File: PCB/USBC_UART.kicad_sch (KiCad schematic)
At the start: 15 parts, among them J1 USB_C_Receptacle_USB2.0_16P, U2 CP2102N-Axx-xQFN20, U3 USBLC6-2SC6

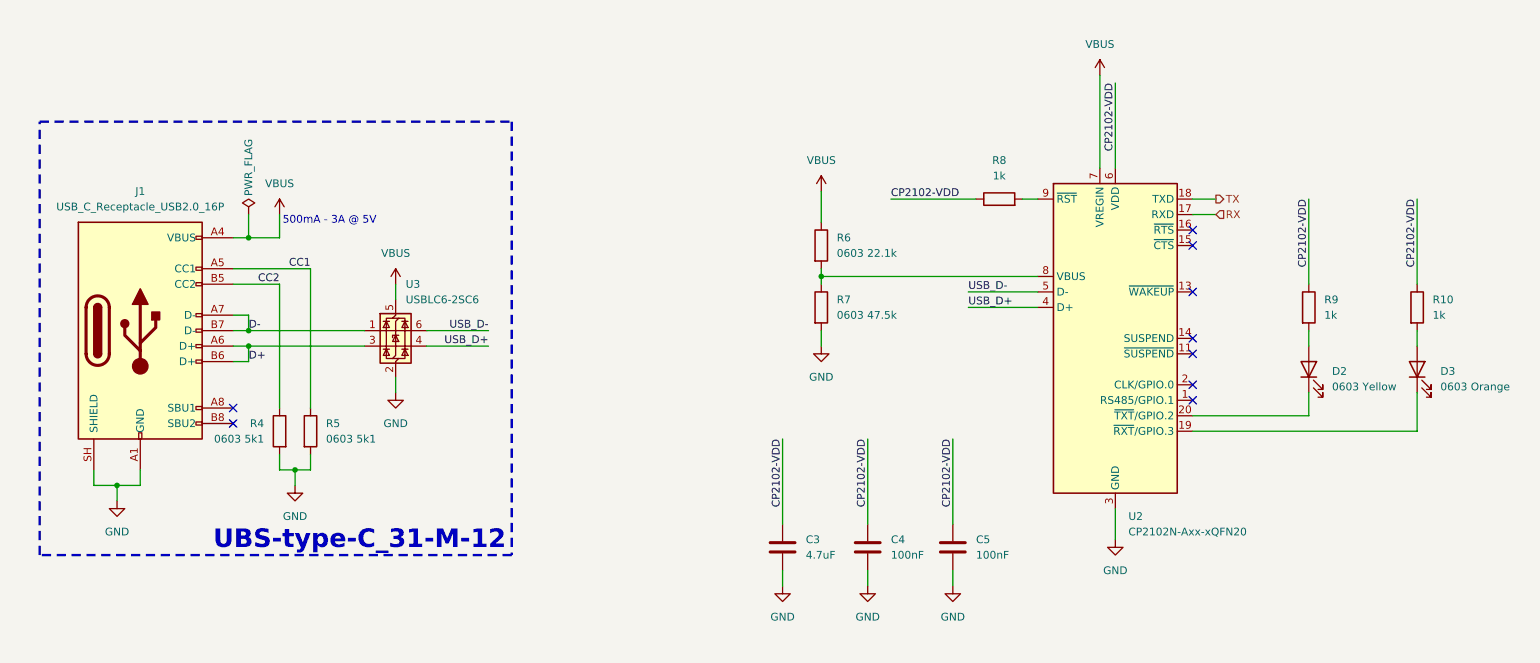
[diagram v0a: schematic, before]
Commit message: added power block, pheripherial
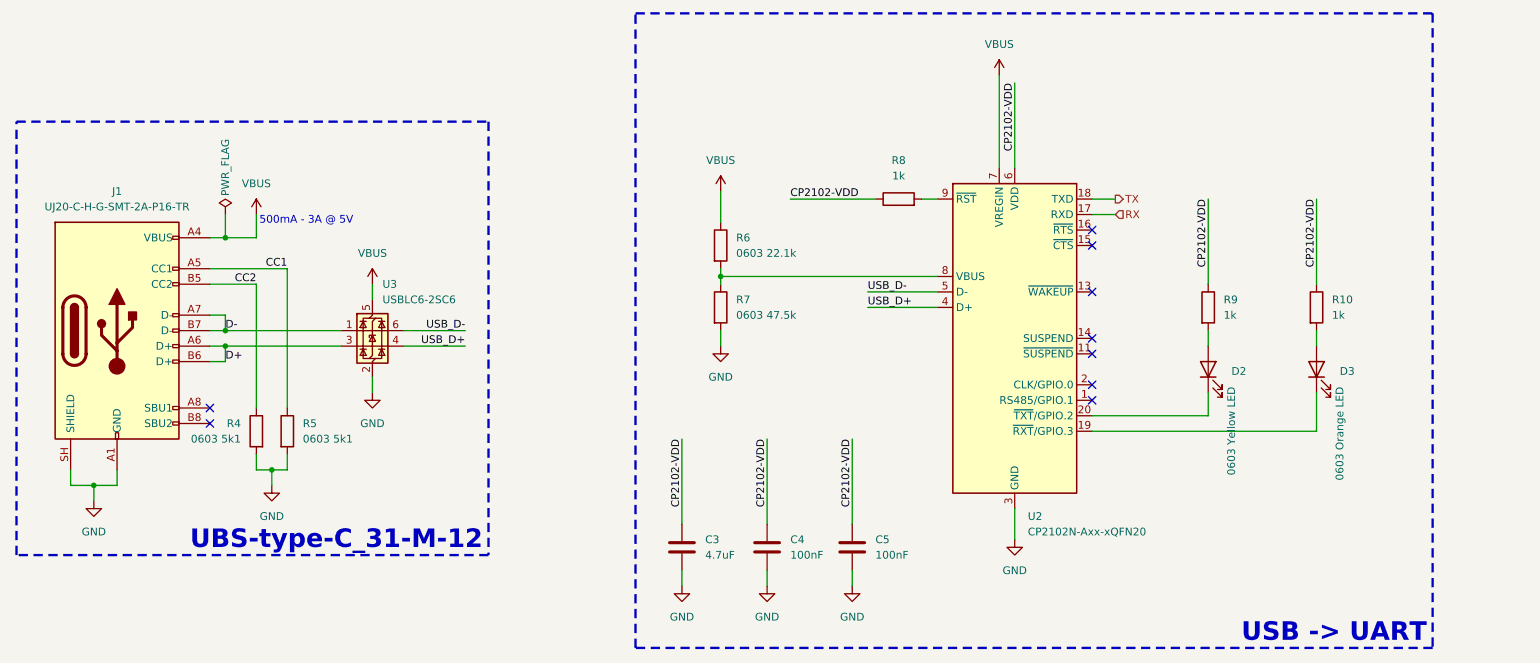
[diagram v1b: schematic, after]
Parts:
- D2: value 0603 Yellow -> 0603 Yellow LED
- D3: value 0603 Orange -> 0603 Orange LED
- J1: value USB_C_Receptacle_USB2.0_16P -> UJ20-C-H-G-SMT-2A-P16-TR
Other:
- moved on the sheet: C3, C4, C5, D2, D3, J1, R10, R4, R5, R6, R7, R8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

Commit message: added GPS, charging IC, SHT41, and started working on the RF
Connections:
- net GND renamed GNDREF
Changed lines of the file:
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@@
 	)
 	(symbol
-		(lib_id "power:GND")
+		(lib_id "power:GNDREF")
 		(at 45.72 114.3 0)
 		(unit 1)
@@
 		(dnp no)
 		(fields_autoplaced yes)
-		(property "Reference" "#PWR07"
+		(property "Reference" "#PWR7"
 			(at 45.72 120.65 0)
 			(hide yes)
@@
 			)
 		)
-		(property "Value" "GND"
+		(property "Value" "GNDREF"
 			(at 45.72 119.38 0)
 			(show_name no)
@@
 			)
 		)
-		(property "Description" "Power symbol creates a global label with name \"GND\" , ground"
+		(property "Description" "Power symbol creates a global label with name \"GNDREF\" , reference supply ground"
 			(at 45.72 114.3 0)
 			(hide yes)
@@
 			(project "PawBuddy_PCB"
 				(path "/ddc031a5-f801-471f-9629-7d18bb02ea71/cad18380-8b9c-4903-b9e2-0a5eb9220f50/58e2bbde-2d8f-48f9-8dad-30c58bb3f27e"
-					(reference "#PWR07")
+					(reference "#PWR7")
 					(unit 1)
 				)
@@
 	)
 	(symbol
-		(lib_id "power:GND")
+		(lib_id "power:GNDREF")
 		(at 148.59 88.9 0)
 		(unit 1)
@@
 		(dnp no)
 		(fields_autoplaced yes)
-		(property "Reference" "#PWR06"
+		(property "Reference" "#PWR6"
 			(at 148.59 95.25 0)
 			(hide yes)
@@
 			)
 		)
-		(property "Value" "GND"
+		(property "Value" "GNDREF"
 			(at 148.59 93.98 0)
 			(show_name no)
@@
 			)
 		)
-		(property "Description" "Power symbol creates a global label with name \"GND\" , ground"
+		(property "Description" "Power symbol creates a global label with name \"GNDREF\" , reference supply ground"
 			(at 148.59 88.9 0)
 			(hide yes)
@@
 			(project "PawBuddy_PCB"
 				(path "/ddc031a5-f801-471f-9629-7d18bb02ea71/cad18380-8b9c-4903-b9e2-0a5eb9220f50/58e2bbde-2d8f-48f9-8dad-30c58bb3f27e"
-					(reference "#PWR06")
+					(reference "#PWR6")
 					(unit 1)
 				)
@@
 	)
 	(symbol
-		(lib_id "power:GND")
+		(lib_id "power:GNDREF")
 		(at 196.85 120.65 0)
 		(unit 1)
@@
 		(dnp no)
 		(fields_autoplaced yes)
-		(property "Reference" "#PWR011"
+		(property "Reference" "#PWR11"
 			(at 196.85 127 0)
 			(hide yes)
@@
 			)
 		)
-		(property "Value" "GND"
+		(property "Value" "GNDREF"
 			(at 196.85 125.73 0)
 			(show_name no)
@@
 			)
 		)
-		(property "Description" "Power symbol creates a global label with name \"GND\" , ground"
+		(property "Description" "Power symbol creates a global label with name \"GNDREF\" , reference supply ground"
 			(at 196.85 120.65 0)
 			(hide yes)
@@
 			(project "PawBuddy_PCB"
 				(path "/ddc031a5-f801-471f-9629-7d18bb02ea71/cad18380-8b9c-4903-b9e2-0a5eb9220f50/58e2bbde-2d8f-48f9-8dad-30c58bb3f27e"
-					(reference "#PWR011")
+					(reference "#PWR11")
 					(unit 1)
 				)
@@
 	)
 	(symbol
-		(lib_id "power:GND")
+		(lib_id "power:GNDREF")
 		(at 156.21 128.27 0)
 		(unit 1)
@@
 		(dnp no)
 		(fields_autoplaced yes)
-		(property "Reference" "#PWR013"
+		(property "Reference" "#PWR13"
 			(at 156.21 134.62 0)
 			(hide yes)
@@
 			)
 		)
-		(property "Value" "GND"
+		(property "Value" "GNDREF"
 			(at 156.21 133.35 0)
 			(show_name no)
@@
 			)
 		)
-		(property "Description" "Power symbol creates a global label with name \"GND\" , ground"
+		(property "Description" "Power symbol creates a global label with name \"GNDREF\" , reference supply ground"
 			(at 156.21 128.27 0)
 			(hide yes)
@@
 			(project "PawBuddy_PCB"
 				(path "/ddc031a5-f801-471f-9629-7d18bb02ea71/cad18380-8b9c-4903-b9e2-0a5eb9220f50/58e2bbde-2d8f-48f9-8dad-30c58bb3f27e"
-					(reference "#PWR013")
-					(unit 1)
-				)
-			)
-		)
-	)
-	(symbol
-		(lib_id "power:GND")
+					(reference "#PWR13")
+					(unit 1)
+				)
+			)
+		)
+	)
+	(symbol
+		(lib_id "power:GNDREF")
 		(at 142.24 128.27 0)
 		(unit 1)
@@
 		(dnp no)
 		(fields_autoplaced yes)
-		(property "Reference" "#PWR012"
+		(property "Reference" "#PWR12"
 			(at 142.24 134.62 0)
 			(hide yes)
@@
 			)
 		)
-		(property "Value" "GND"
+		(property "Value" "GNDREF"
 			(at 142.24 133.35 0)
 			(show_name no)
@@
 			)
 		)
-		(property "Description" "Power symbol creates a global label with name \"GND\" , ground"
+		(property "Description" "Power symbol creates a global label with name \"GNDREF\" , reference supply ground"
 			(at 142.24 128.27 0)
 			(hide yes)
@@
 			(project "PawBuddy_PCB"
 				(path "/ddc031a5-f801-471f-9629-7d18bb02ea71/cad18380-8b9c-4903-b9e2-0a5eb9220f50/58e2bbde-2d8f-48f9-8dad-30c58bb3f27e"
-					(reference "#PWR012")
+					(reference "#PWR12")
 					(unit 1)
 				)
@@
 	)
 	(symbol
-		(lib_id "power:GND")
+		(lib_id "power:GNDREF")
 		(at 74.93 111.76 0)
 		(unit 1)
@@
 		(dnp no)
 		(fields_autoplaced yes)
-		(property "Reference" "#PWR09"
+		(property "Reference" "#PWR9"
 			(at 74.93 118.11 0)
 			(hide yes)
@@
 			)
 		)
-		(property "Value" "GND"
+		(property "Value" "GNDREF"
 			(at 74.93 116.84 0)
 			(show_name no)
@@
 			)
 		)
-		(property "Description" "Power symbol creates a global label with name \"GND\" , ground"
+		(property "Description" "Power symbol creates a global label with name \"GNDREF\" , reference supply ground"
 			(at 74.93 111.76 0)
 			(hide yes)
@@
 			(project "PawBuddy_PCB"
 				(path "/ddc031a5-f801-471f-9629-7d18bb02ea71/cad18380-8b9c-4903-b9e2-0a5eb9220f50/58e2bbde-2d8f-48f9-8dad-30c58bb3f27e"
-					(reference "#PWR09")
-					(unit 1)
-				)
-			)
-		)
-	)
-	(symbol
-		(lib_id "power:GND")
+					(reference "#PWR9")
+					(unit 1)
+				)
+			)
+		)
+	)
+	(symbol
+		(lib_id "power:GNDREF")
 		(at 170.18 128.27 0)
 		(unit 1)
@@
 		(dnp no)
 		(fields_autoplaced yes)
-		(property "Reference" "#PWR014"
+		(property "Reference" "#PWR14"
 			(at 170.18 134.62 0)
 			(hide yes)
@@
 			)
 		)
-		(property "Value" "GND"
+		(property "Value" "GNDREF"
 			(at 170.18 133.35 0)
 			(show_name no)
@@
 			)
 		)
-		(property "Description" "Power symbol creates a global label with name \"GND\" , ground"
+		(property "Description" "Power symbol creates a global label with name \"GNDREF\" , reference supply ground"
 			(at 170.18 128.27 0)
 			(hide yes)
@@
 			(project "PawBuddy_PCB"
 				(path "/ddc031a5-f801-471f-9629-7d18bb02ea71/cad18380-8b9c-4903-b9e2-0a5eb9220f50/58e2bbde-2d8f-48f9-8dad-30c58bb3f27e"
-					(reference "#PWR014")
+					(reference "#PWR14")
 					(unit 1)
 				)
@@
 	)
 	(symbol
-		(lib_id "power:GND")
+		(lib_id "power:GNDREF")
 		(at 91.44 96.52 0)
 		(unit 1)
@@
 		(dnp no)
 		(fields_autoplaced yes)
-		(property "Reference" "#PWR015"
+		(property "Reference" "#PWR15"
 			(at 91.44 102.87 0)
 			(hide yes)
@@
 			)
 		)
-		(property "Value" "GND"
+		(property "Value" "GNDREF"
 			(at 91.44 101.6 0)
 			(show_name no)
@@
 			)
 		)
-		(property "Description" "Power symbol creates a global label with name \"GND\" , ground"
+		(property "Description" "Power symbol creates a global label with name \"GNDREF\" , reference supply ground"
 			(at 91.44 96.52 0)
 			(hide yes)
@@
 			(project "PawBuddy_PCB"
 				(path "/ddc031a5-f801-471f-9629-7d18bb02ea71/cad18380-8b9c-4903-b9e2-0a5eb9220f50/58e2bbde-2d8f-48f9-8dad-30c58bb3f27e"
-					(reference "#PWR015")
-					(unit 1)
-				)
+					(reference "#PWR15")
+					(unit 1)
+				)
